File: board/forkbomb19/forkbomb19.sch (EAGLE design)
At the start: 55 parts, among them SW1 SPST_TACT-KMR2, U1 ESP-WROOM-03, X3 POT_GND, X4 POT_3V3, X5 POT_SIG

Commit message: moving to lithium batteries
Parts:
- removed BATT: 22-23-2021, con-molex:22-23-2021
- removed C11: 4.7pF, resistor:C-USC0603
- removed C12: 100uF, resistor:CPOL-USC/6032-28R
- removed D1, D2: MBRS130LT3, diode:MBRS130LT3
- removed L1: 4.7uH, resistor:L-USWE-TPC
- removed R10: 165k, resistor:R-US_R0603
- removed R11: 100k, resistor:R-US_R0603
- removed U$1: LM2623, forkbomb19:LM2623
- added B1: JST 2-PH, microbuilder:BATTERY
- added C15: 2.2uF, rcl:C-USC0805
- added C16: 0.1uF, microbuilder:CAP_CERAMIC0805_10MGAP
- added C2: 10uF, microbuilder:CAP_CERAMIC0805-NOOUTLINE
- added CHRG/LBO: ORANGE, microbuilder:LED0805_NOOUTLINE
- added DONE: GREEN, microbuilder:LED0805_NOOUTLINE
- added L2: 6.8uH, microbuilder:INDUCTORTDK_VLC5045
- added LED1: RED, microbuilder:LED0805_NOOUTLINE
- added R18, R21: 200K, rcl:R-US_R0603
- added R19: 1.12M, rcl:R-US_R0603
- added R20, R27, R28: 1K, rcl:R-US_R0603
- added R23: 340K, rcl:R-US_R0603
- added R24: 1.87M, rcl:R-US_R0603
- added R25: 270K, rcl:R-US_R0603
- added R26, R30: 100K, rcl:R-US_R0603
- added R29: 1.0K, rcl:R-US_R0603
- added T3: MMUN2133LT1G, transistor:MUN2114T1-PNP_DRIVER-SC59-BEC
- added THERM: 15K, rcl:R-US_R0603
- added U4: TPS61090RSAR, microbuilder:VREG_TPS6103X
- added U5: MCP73871, microbuilder:MCP73871
- C10: value 22uF -> 100uF; device resistor:CPOL-USB/3528-21R -> rcl:CPOL-USC/6032-28R
- R9: value 150k -> 200k; device resistor:R-US_R0603 -> rcl:R-US_R0603
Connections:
- removed net N$14: C11.2, R9.1, U$1.FREQ
- removed net N$15: C11.1, D2.A, L1.2, U$1.SW
- removed net N$17: U$1.EN, U$17.P$2
- removed net N$18: R10.1, R11.2, U$1.FB
- removed net N$30: BATT-1.S, D1.A
- new net ENABLE: U$17.P$2, U4.EN
- new net LBO: T3.B, U4.LBO
- new net N$16: L2.2, U4.SW
- new net N$23: R23.2, R24.1, U4.LBI
- new net N$24: LED1.A, R20.1
- new net N$25: R19.1, R21.2, U4.FB
- new net N$26: R20.2, T3.C
- new net N$28: R25.1, R26.1, U5.VPCC
- new net N$29: R28.1, U5.STAT2
- new net N$32: R27.1, U5.STAT1/LBO
- new net N$33: R29.2, U5.PROG1
- new net N$34: THERM.2, U5.THERM
- new net N$35: DONE.C, R28.2
- new net N$36: CHRG/LBO.C, R27.2
- new net N$37: R30.2, U5.PROG3
- new net N$42: R18.2, U$17.P$3
- new net VBAT: C16.1, C2.1, L2.1, R18.1, R24.2, T3.E, U4.VBAT, U5.VOUT1, U5.VOUT2
- new net VBUS: CHRG/LBO.A, DONE.A, R25.2, U5./TE, U5.CE, U5.PROG2, U5.SEL, U5.VIN1, U5.VIN2
- new net VLIPO: B1.+, C10.+, U5.VBAT1, U5.VBAT2, U5.VBATSENS
- net +3V3: now also C15.1, R19.2, U4.VOUT; no longer C12.+, D2.C, R10.2, U$1.BOOT, U$1.VDD, U$17.P$3
- net GND: now also B1.-, C15.2, C16.2, C2.2, LED1.C, R21.1, R23.1, R26.2, R29.1, R30.1, R9.2, THERM.1, U4.GND, U4.PGND, U4.SYNC, U5.THERMAL, U5.VSS1, U5.VSS2; no longer BATT-2.S, C12.-, R11.1, U$1.PGND, U$1.SGND, U$17.P$1
- net N$13: now also R9.1, U$17.P$1; no longer C10.+, D1.C, L1.1, R9.2
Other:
- note added: "On/Off Switch"
- moved on the sheet: C10, C3, LOGO_B, LOGO_G, LOGO_R, R22, R8, R9, TOUCH

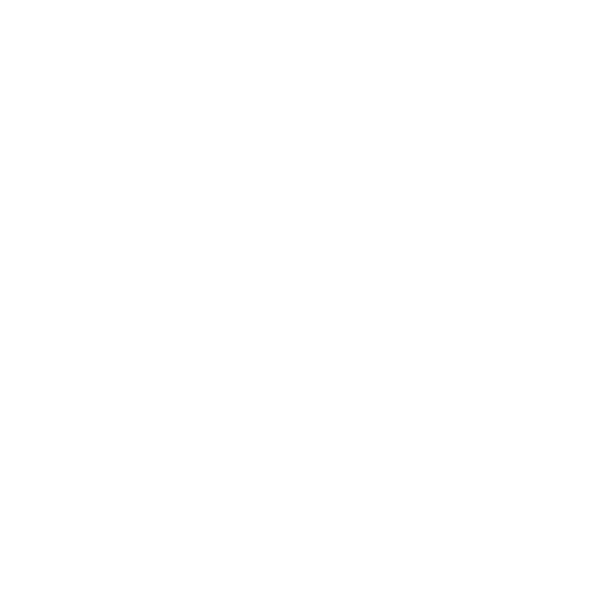
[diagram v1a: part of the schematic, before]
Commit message: added new thermal sensor part
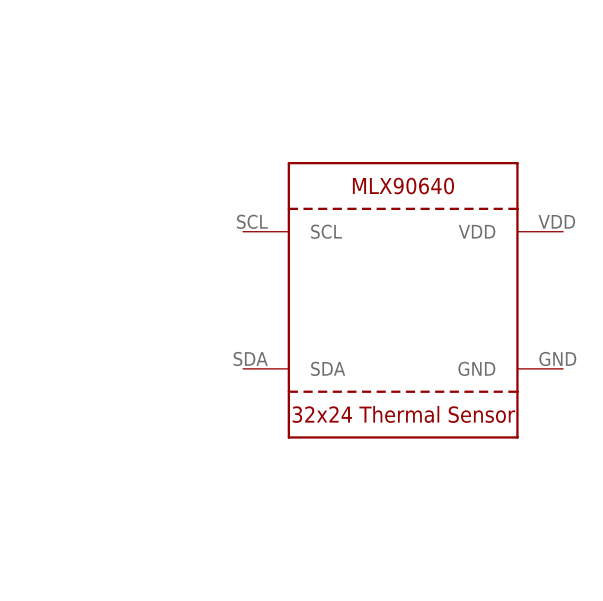
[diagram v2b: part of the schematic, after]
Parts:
- added U$7: MLX90640, forkbomb19:MLX90640
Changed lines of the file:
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@@
 <part name="U$1" library="microbuilder" deviceset="GND" device=""/>
 <part name="C10" library="rcl" library_urn="urn:adsk.eagle:library:334" deviceset="CPOL-US" device="C/6032-28R" package3d_urn="urn:adsk.eagle:package:23415/1" value="100uF"/>
+<part name="U$7" library="forkbomb19" deviceset="MLX90640" device=""/>
 </parts>
 <sheets>
@@
 <attribute name="VALUE" x="-77.724" y="-82.931" size="1.778" layer="96"/>
 </instance>
+<instance part="U$7" gate="G$1" x="233.68" y="-17.78" smashed="yes"/>
 </instances>
 <busses>

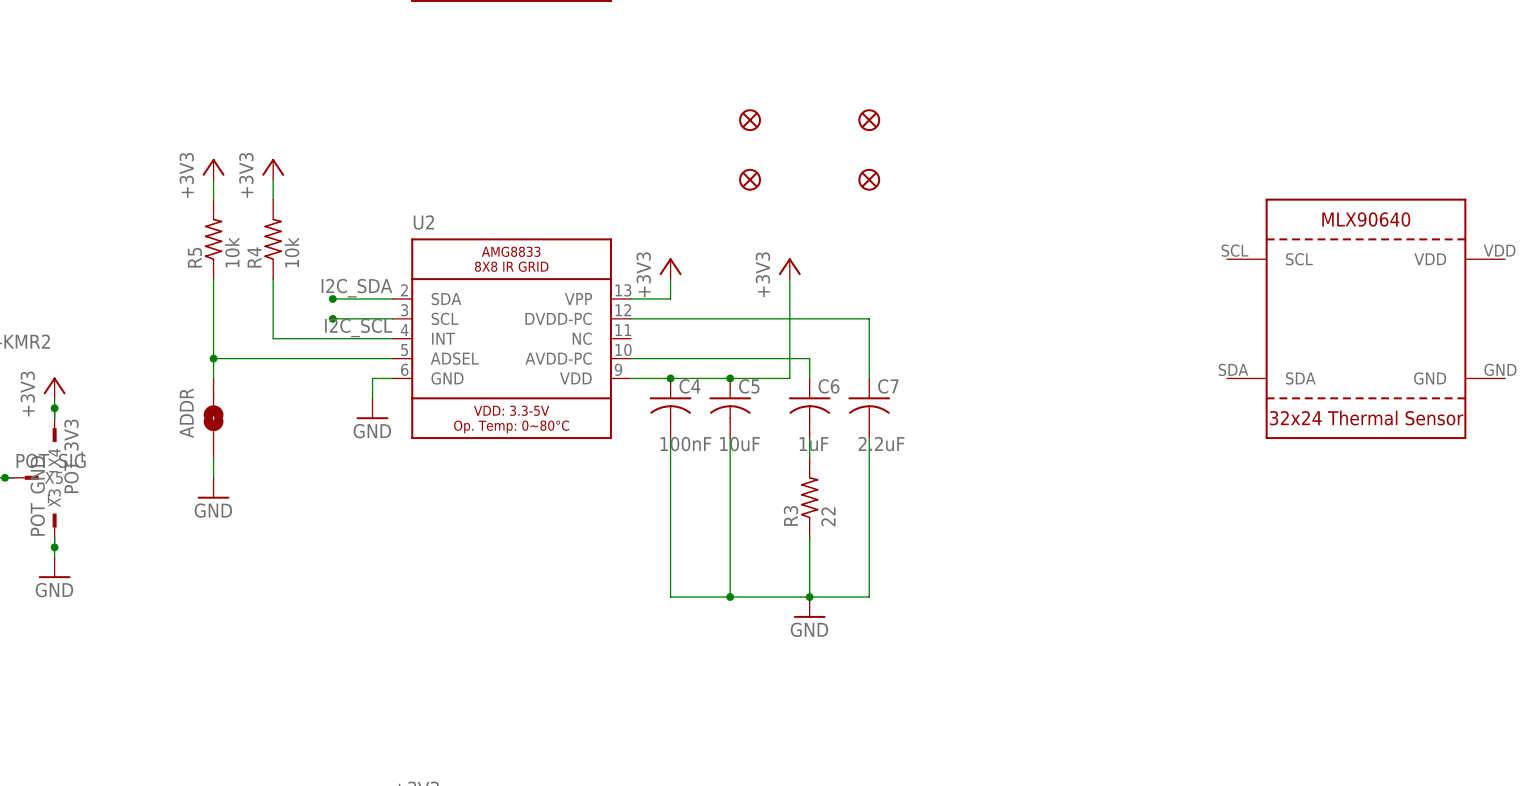
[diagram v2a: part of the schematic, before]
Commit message: added thermal sensor to the board
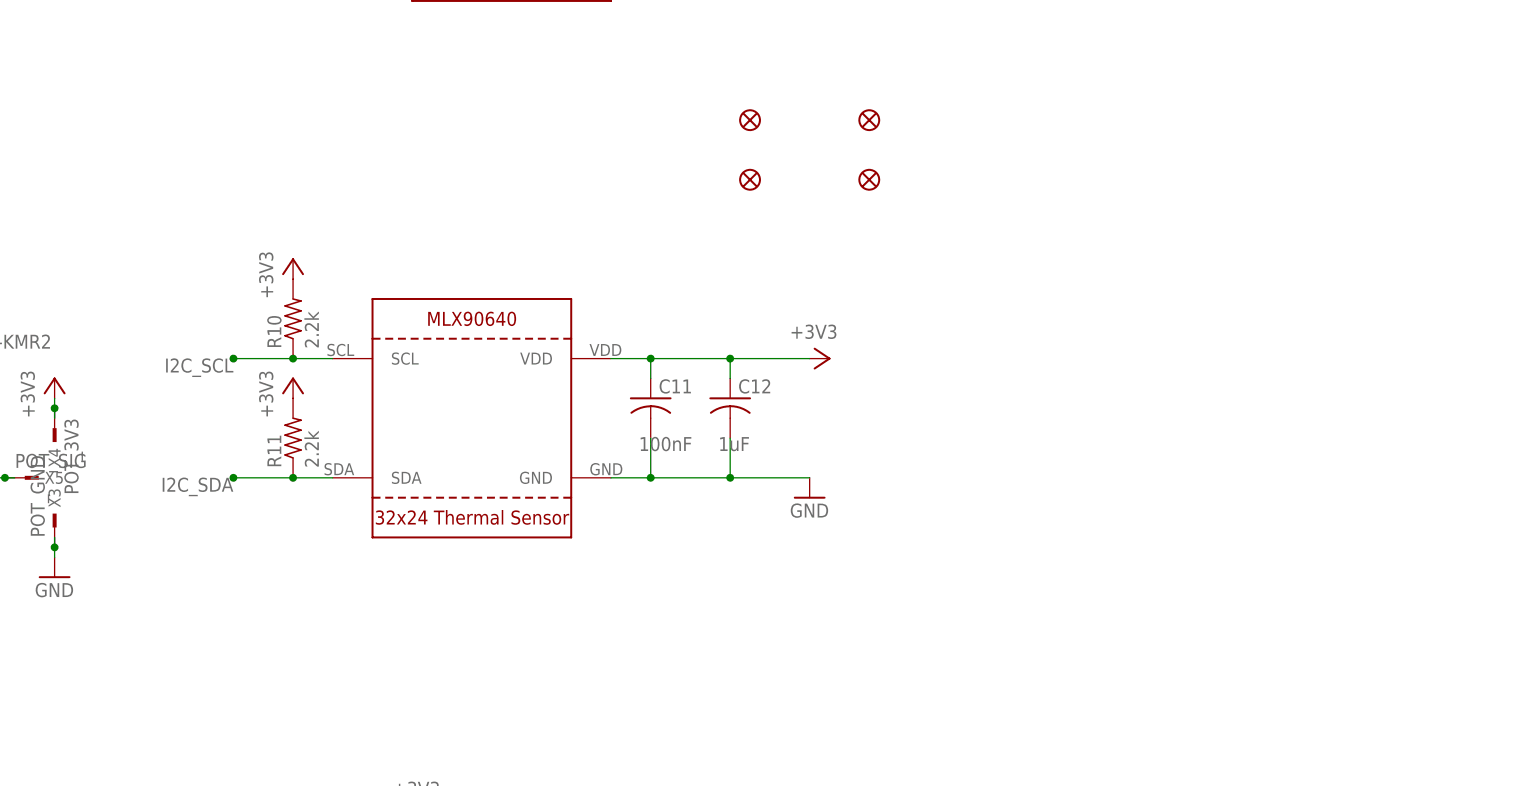
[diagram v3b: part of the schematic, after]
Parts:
- removed ADDR: JUMPER-SMT_2_NO_SILK_ROUND, SparkFun-Jumpers:JUMPER-SMT_2_NO_SILK_ROUND
- removed C4: 100nF, resistor:C-USC0603
- removed C6: 1uF, resistor:C-USC0805
- removed C7: 2.2uF, resistor:C-USC0805
- removed R3: 22, resistor:R-US_R0805
- removed R4, R5: 10k, resistor:R-US_R0805
- removed U2: (no value), forkbomb19:MICROBUILDER_AMG8833
- added C11: 100nF, resistor:C-USC0603
- added R10, R11: 2.2k, resistor:R-US_R0603
- C12: value 10uF -> 1uF
- renumbered C5 to C12
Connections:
- removed net N$10: C6.2, R3.2
- removed net N$11: R4.1, U2.INT
- removed net N$7: ADDR.2, R5.1, U2.ADSEL
- removed net N$8: C6.1, U2.AVDD-PC
- removed net N$9: C7.1, U2.DVDD-PC
- net +3V3: now also C11.1, R10.2, R11.2, U$7.VDD; no longer C4.1, R4.2, R5.2, U2.VDD, U2.VPP
- net GND: now also C11.2, U$7.GND; no longer ADDR.1, C4.2, C7.2, R3.1, U2.GND
- net I2C_SCL: now also R10.1, U$7.SCL; no longer U2.SCL
- net I2C_SDA: now also R11.1, U$7.SDA; no longer U2.SDA

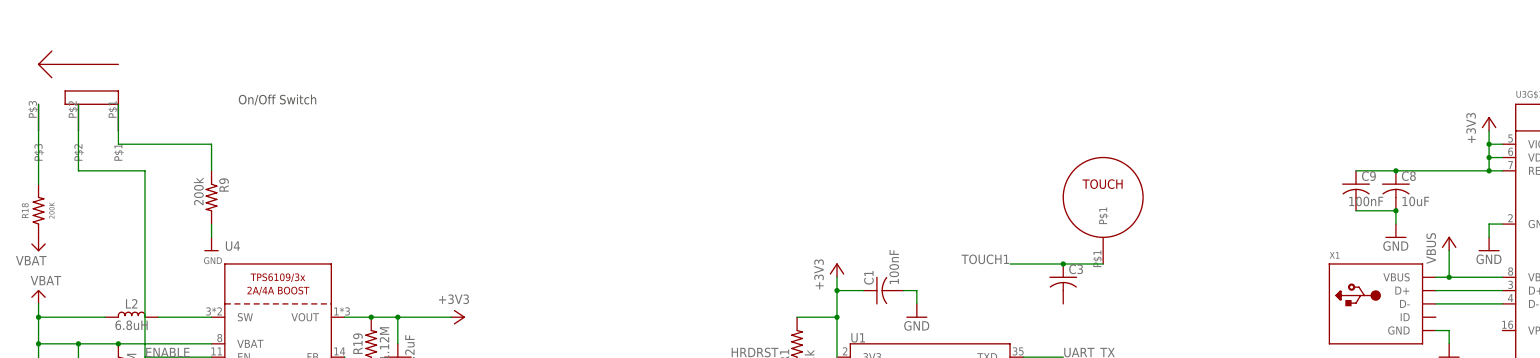
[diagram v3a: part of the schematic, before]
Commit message: footprint pretty much done, needs cleanup
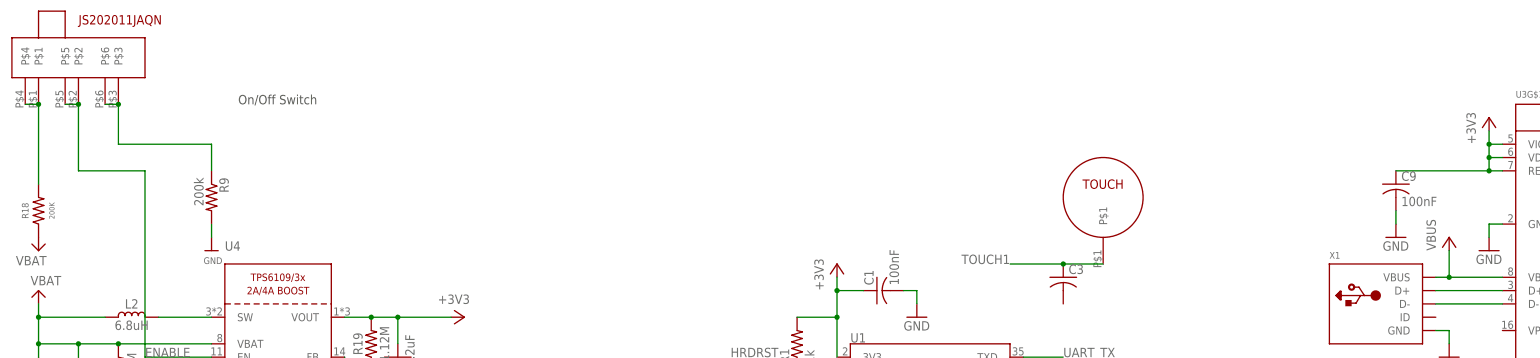
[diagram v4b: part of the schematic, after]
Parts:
- removed C8: 10uF, resistor:C-USC0805
- removed U$17: CL-SB-12A-02T, defcon:CL-SB-12A-02T
- added U$8: JS202011JAQN, forkbomb19:JS202011JAQN
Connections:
- removed net +5V: U3G$1.VBUS, X1.VBUS
- net +3V3: no longer C8.1
- net ENABLE: now also U$8.P$2, U$8.P$5; no longer U$17.P$2
- net GND: no longer C8.2
- net N$13: now also U$8.P$3, U$8.P$6; no longer U$17.P$1
- net N$42: now also U$8.P$1, U$8.P$4; no longer U$17.P$3
- net VBUS: now also U3G$1.VBUS, X1.VBUS
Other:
- moved on the sheet: C9
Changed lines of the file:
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@@
 <part name="GND10" library="supply1" library_urn="urn:adsk.eagle:library:371" deviceset="GND" device=""/>
 <part name="P+1" library="supply1" library_urn="urn:adsk.eagle:library:371" deviceset="+5V" device="" value="VBUS"/>
-<part name="C8" library="resistor" library_urn="urn:adsk.eagle:library:348" deviceset="C-US" device="C0805" package3d_urn="urn:adsk.eagle:package:23617/2" value="10uF"/>
 <part name="GND11" library="supply1" library_urn="urn:adsk.eagle:library:371" deviceset="GND" device=""/>
 <part name="+3V7" library="supply1" library_urn="urn:adsk.eagle:library:371" deviceset="+3V3" device=""/>
@@
 <part name="LOGO_G" library="forkbomb19" deviceset="REVERSE_PLCC_LED" device="" value=""/>
 <part name="LOGO_B" library="forkbomb19" deviceset="REVERSE_PLCC_LED" device="" value=""/>
-<part name="U$17" library="defcon" deviceset="CL-SB-12A-02T" device=""/>
 <part name="GND12" library="supply1" library_urn="urn:adsk.eagle:library:371" deviceset="GND" device=""/>
 <part name="+3V8" library="supply1" library_urn="urn:adsk.eagle:library:371" deviceset="+3V3" device=""/>
@@
 <part name="+3V15" library="supply1" library_urn="urn:adsk.eagle:library:371" deviceset="+3V3" device=""/>
 <part name="+3V16" library="supply1" library_urn="urn:adsk.eagle:library:371" deviceset="+3V3" device=""/>
+<part name="U$8" library="forkbomb19" deviceset="JS202011JAQN" device=""/>
 </parts>
 <sheets>
@@
 </instance>
 <instance part="P+1" gate="1" x="99.06" y="55.88" smashed="yes">
-<attribute name="VALUE" x="96.52" y="50.8" size="1.778" layer="96" rot="R90"/>
-</instance>
-<instance part="C8" gate="G$1" x="88.9" y="66.04" smashed="yes">
+<attribute name="VALUE" x="96.52" y="53.34" size="1.778" layer="96" rot="R90"/>
+</instance>
+<instance part="GND11" gate="1" x="88.9" y="55.88" smashed="yes">
+<attribute name="VALUE" x="86.36" y="53.34" size="1.778" layer="96"/>
+</instance>
+<instance part="+3V7" gate="G$1" x="106.68" y="78.74" smashed="yes">
+<attribute name="VALUE" x="104.14" y="73.66" size="1.778" layer="96" rot="R90"/>
+</instance>
+<instance part="C9" gate="G$1" x="88.9" y="66.04" smashed="yes">
 <attribute name="NAME" x="89.916" y="66.675" size="1.778" layer="95"/>
 <attribute name="VALUE" x="89.916" y="61.849" size="1.778" layer="96"/>
-</instance>
-<instance part="GND11" gate="1" x="88.9" y="55.88" smashed="yes">
-<attribute name="VALUE" x="86.36" y="53.34" size="1.778" layer="96"/>
-</instance>
-<instance part="+3V7" gate="G$1" x="106.68" y="78.74" smashed="yes">
-<attribute name="VALUE" x="104.14" y="73.66" size="1.778" layer="96" rot="R90"/>
-</instance>
-<instance part="C9" gate="G$1" x="81.28" y="66.04" smashed="yes">
-<attribute name="NAME" x="82.296" y="66.675" size="1.778" layer="95"/>
-<attribute name="VALUE" x="79.756" y="61.849" size="1.778" layer="96"/>
 </instance>
 <instance part="T1" gate="G$1" x="208.28" y="33.02" smashed="yes" rot="R270">
@@
 <attribute name="VALUE" x="84.328" y="-102.235" size="1.778" layer="96"/>
 </instance>
-<instance part="U$17" gate="G$1" x="-162.56" y="83.82" smashed="yes" rot="MR0"/>
 <instance part="GND12" gate="1" x="71.12" y="-101.6" smashed="yes">
 <attribute name="VALUE" x="68.58" y="-104.14" size="1.778" layer="96"/>
@@
 <attribute name="VALUE" x="93.98" y="-30.48" size="1.778" layer="96" rot="R90"/>
 </instance>
+<instance part="U$8" gate="G$1" x="-162.56" y="86.36" smashed="yes"/>
 </instances>
 <busses>
@@
 <wire x1="106.68" y1="68.58" x2="88.9" y2="68.58" width="0.1524" layer="91"/>
 <junction x="106.68" y="68.58"/>
-<pinref part="C8" gate="G$1" pin="1"/>
 <pinref part="+3V7" gate="G$1" pin="+3V3"/>
 <wire x1="106.68" y1="73.66" x2="106.68" y2="76.2" width="0.1524" layer="91"/>
 <junction x="106.68" y="73.66"/>
 <pinref part="C9" gate="G$1" pin="1"/>
-<wire x1="88.9" y1="68.58" x2="81.28" y2="68.58" width="0.1524" layer="91"/>
-<junction x="88.9" y="68.58"/>
 </segment>
 <segment>
@@
 </segment>
 <segment>
-<pinref part="C8" gate="G$1" pin="2"/>
 <pinref part="GND11" gate="1" pin="GND"/>
 <wire x1="88.9" y1="60.96" x2="88.9" y2="58.42" width="0.1524" layer="91"/>
 <pinref part="C9" gate="G$1" pin="2"/>
-<wire x1="88.9" y1="60.96" x2="81.28" y2="60.96" width="0.1524" layer="91"/>
-<junction x="88.9" y="60.96"/>
 </segment>
 <segment>
@@
 </segment>
 </net>
-<net name="+5V" class="0">
-<segment>
-<pinref part="X1" gate="G$1" pin="VBUS"/>
-<pinref part="U3" gate="G$1" pin="VBUS"/>
-<wire x1="96.52" y1="48.26" x2="99.06" y2="48.26" width="0.1524" layer="91"/>
-<pinref part="P+1" gate="1" pin="+5V"/>
-<wire x1="99.06" y1="48.26" x2="109.22" y2="48.26" width="0.1524" layer="91"/>
-<wire x1="99.06" y1="53.34" x2="99.06" y2="48.26" width="0.1524" layer="91"/>
-<junction x="99.06" y="48.26"/>
-</segment>
-</net>
 <net name="UART_RX" class="0">
 <segment>
@@
 <wire x1="-149.86" y1="33.02" x2="-149.86" y2="68.58" width="0.1524" layer="91"/>
 <wire x1="-149.86" y1="68.58" x2="-162.56" y2="68.58" width="0.1524" layer="91"/>
-<pinref part="U$17" gate="G$1" pin="P$2"/>
 <wire x1="-162.56" y1="68.58" x2="-162.56" y2="81.28" width="0.1524" layer="91"/>
+<pinref part="U$8" gate="G$1" pin="P$2"/>
+<pinref part="U$8" gate="G$1" pin="P$5"/>
+<wire x1="-162.56" y1="81.28" x2="-165.1" y2="81.28" width="0.1524" layer="91"/>
+<junction x="-162.56" y="81.28"/>
 </segment>
 </net>
@@
 <wire x1="-157.48" y1="-43.18" x2="-157.48" y2="-38.1" width="0.1524" layer="91"/>
 </segment>
+<segment>
+<pinref part="X1" gate="G$1" pin="VBUS"/>
+<pinref part="U3" gate="G$1" pin="VBUS"/>
+<wire x1="96.52" y1="48.26" x2="99.06" y2="48.26" width="0.1524" layer="91"/>
+<pinref part="P+1" gate="1" pin="+5V"/>
+<wire x1="99.06" y1="48.26" x2="109.22" y2="48.26" width="0.1524" layer="91"/>
+<wire x1="99.06" y1="53.34" x2="99.06" y2="48.26" width="0.1524" layer="91"/>
+<junction x="99.06" y="48.26"/>
+</segment>
 </net>
 <net name="VLIPO" class="0">
@@
 <net name="N$42" class="0">
 <segment>
-<pinref part="U$17" gate="G$1" pin="P$3"/>
 <wire x1="-170.18" y1="81.28" x2="-170.18" y2="66.04" width="0.1524" layer="91"/>
 <pinref part="R18" gate="G$1" pin="2"/>
+<pinref part="U$8" gate="G$1" pin="P$1"/>
+<pinref part="U$8" gate="G$1" pin="P$4"/>
+<wire x1="-170.18" y1="81.28" x2="-172.72" y2="81.28" width="0.1524" layer="91"/>
+<junction x="-170.18" y="81.28"/>
 </segment>
 </net>
 <net name="N$13" class="0">
 <segment>
-<pinref part="U$17" gate="G$1" pin="P$1"/>
 <wire x1="-154.94" y1="81.28" x2="-154.94" y2="73.66" width="0.1524" layer="91"/>
 <wire x1="-154.94" y1="73.66" x2="-137.16" y2="73.66" width="0.1524" layer="91"/>
 <wire x1="-137.16" y1="73.66" x2="-137.16" y2="68.58" width="0.1524" layer="91"/>
 <pinref part="R9" gate="G$1" pin="1"/>
-</segment>
-</net>
+<pinref part="U$8" gate="G$1" pin="P$3"/>
+<pinref part="U$8" gate="G$1" pin="P$6"/>
+<wire x1="-154.94" y1="81.28" x2="-157.48" y2="81.28" width="0.1524" layer="91"/>
+<junction x="-154.94" y="81.28"/>
+</segment>
+</net>
